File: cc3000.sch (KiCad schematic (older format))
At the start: 7 parts, among them P1 CONN_4X2, U1 U.FL_U.FL, U2 CC3000TEXAS_CC3000

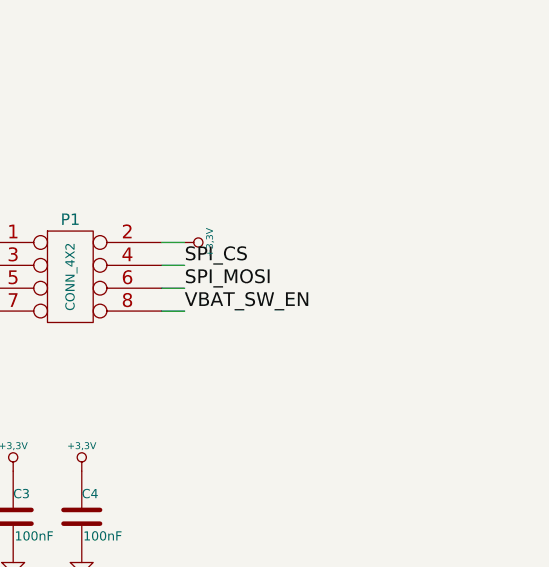
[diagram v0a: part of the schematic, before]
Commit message: pinheader for breadboard
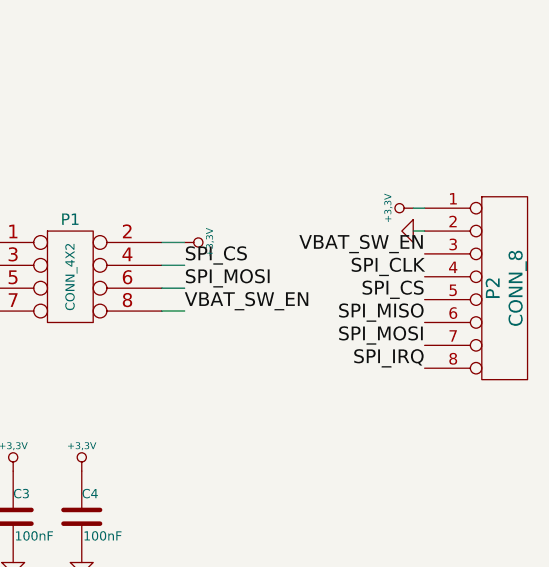
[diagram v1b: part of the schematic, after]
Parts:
- added P2: CONN_8, symbol CONN_8
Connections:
- net +3.3V: now also P2.1 (P1)
- net GND: now also P2.2 (P2)
- net SPI_CLK: now also P2.4 (P4)
- net SPI_CS: now also P2.5 (P5)
- net SPI_IRQ: now also P2.8 (P8)
- net SPI_MISO: now also P2.6 (P6)
- net SPI_MOSI: now also P2.7 (P7)
- net VBAT_SW_EN: now also P2.3 (P3)
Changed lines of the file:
@@
-EESchema Schematic File Version 2
+EESchema Schematic File Version 2  date 20/07/2013 02:36:30
 LIBS:power
 LIBS:device
@@
 Sheet 2 2
 Title ""
-Date ""
+Date "20 jul 2013"
 Rev ""
 Comp ""
@@
 Text Label 4550 2250 0    60   ~ 0
 antena2
+$Comp
+L CONN_8 P2
+U 1 1 51E9E89C
+P 9800 3700
+F 0 "P2" V 9750 3700 60  0000 C CNN
+F 1 "CONN_8" V 9850 3700 60  0000 C CNN
+F 2 "" H 9800 3700 60  0000 C CNN
+F 3 "" H 9800 3700 60  0000 C CNN
+	1    9800 3700
+	1    0    0    -1
+$EndComp
+$Comp
+L +3,3V #PWR024
+U 1 1 51E9E8F9
+P 9400 3350
+F 0 "#PWR024" H 9400 3310 30  0001 C CNN
+F 1 "+3,3V" H 9400 3460 30  0000 C CNN
+F 2 "" H 9400 3350 60  0000 C CNN
+F 3 "" H 9400 3350 60  0000 C CNN
+	1    9400 3350
+	0    -1   -1   0
+$EndComp
+$Comp
+L GND #PWR025
+U 1 1 51E9E8FF
+P 9400 3450
+F 0 "#PWR025" H 9400 3450 30  0001 C CNN
+F 1 "GND" H 9400 3380 30  0001 C CNN
+F 2 "" H 9400 3450 60  0000 C CNN
+F 3 "" H 9400 3450 60  0000 C CNN
+	1    9400 3450
+	0    1    1    0
+$EndComp
+Text Label 9450 3550 2    60   ~ 0
+VBAT_SW_EN
+Text Label 9450 3650 2    60   ~ 0
+SPI_CLK
+Text Label 9450 3750 2    60   ~ 0
+SPI_CS
+Text Label 9450 3850 2    60   ~ 0
+SPI_MISO
+Text Label 9450 3950 2    60   ~ 0
+SPI_MOSI
+Text Label 9450 4050 2    60   ~ 0
+SPI_IRQ
+Wire Wire Line
+	9450 3350 9400 3350
+Wire Wire Line
+	9450 3450 9400 3450
 $EndSCHEMATC
